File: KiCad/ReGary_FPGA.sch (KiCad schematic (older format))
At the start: 26 parts, among them U1 10M02SCU169C8G, U2 LM1117-3.3

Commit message: Removed BGA FPGA
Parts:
- removed U1: 10M02SCU169C8G, ReGary:BGA-169_11.0x11.0mm_Layout13x13_P0.8mm_Ball0.5mm_Pad0.35mm_NSMD, symbol ReGary:10M02SCU169
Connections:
- net labels removed: A0_FPGA, A1_FPGA, A2_FPGA, A3_FPGA, ABOE0_FPGA, ABOE1_FPGA, ABOE2_FPGA, ADDRZ3_FPGA, AS_FPGA, BERR_FPGA, BGACK_FPGA, BG_FPGA, BIGZ_FPGA, BINT_FPGA, BR_FPGA, C7M_FPGA, CBACK_FPGA, CBREQ_FPGA, CCS_FPGA, CDAC_FPGA, CIIN_FPGA, CINH_FPGA, CLK90_FPGA, CPUCLK_FPGA, D2P_FPGA, DBLT_FPGA, DBOE0_FPGA, DBOE1_FPGA, DBR16_FPGA, DOE_FPGA, DSACK0_FPGA, DSACK1_FPGA, DS_FPGA, DTACK_FPGA, EA2_FPGA, EA3_FPGA, EBCLR_FPGA, EBG0_FPGA, EBG1_FPGA, EBG2_FPGA, EBG3_FPGA, EBG4_FPGA, EBGACK_FPGA, EBR0_FPGA, EBR1_FPGA, EBR2_FPGA, EBR3_FPGA, EBR4_FPGA, EDS0_FPGA, EDS1_FPGA, EDS2_FPGA, EDS3_FPGA, FCS_FPGA, HLT_FPGA, IOZ2_FPGA, LOCK_EA1_FPGA, MEMZ2_FPGA, MS0_FPGA, MS1_FPGA, MS2_FPGA, MTACK_FPGA, MTCR_FPGA, OWN_FPGA, READ_FPGA, RESET_FPGA, RMC_FPGA, RW_FPGA, SBG_FPGA, SBR_FPGA, SIZ0_FPGA, SIZ1_FPGA, SLAVE0_FPGA, SLAVE1_FPGA, SLAVE2_FPGA, SLAVE3_FPGA, SLAVE4_FPGA, STERM_FPGA, WAIT_FPGA
- wire segments 82 -> 42
- no-connect marks 24 -> 3
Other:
- moved on the sheet: TP1

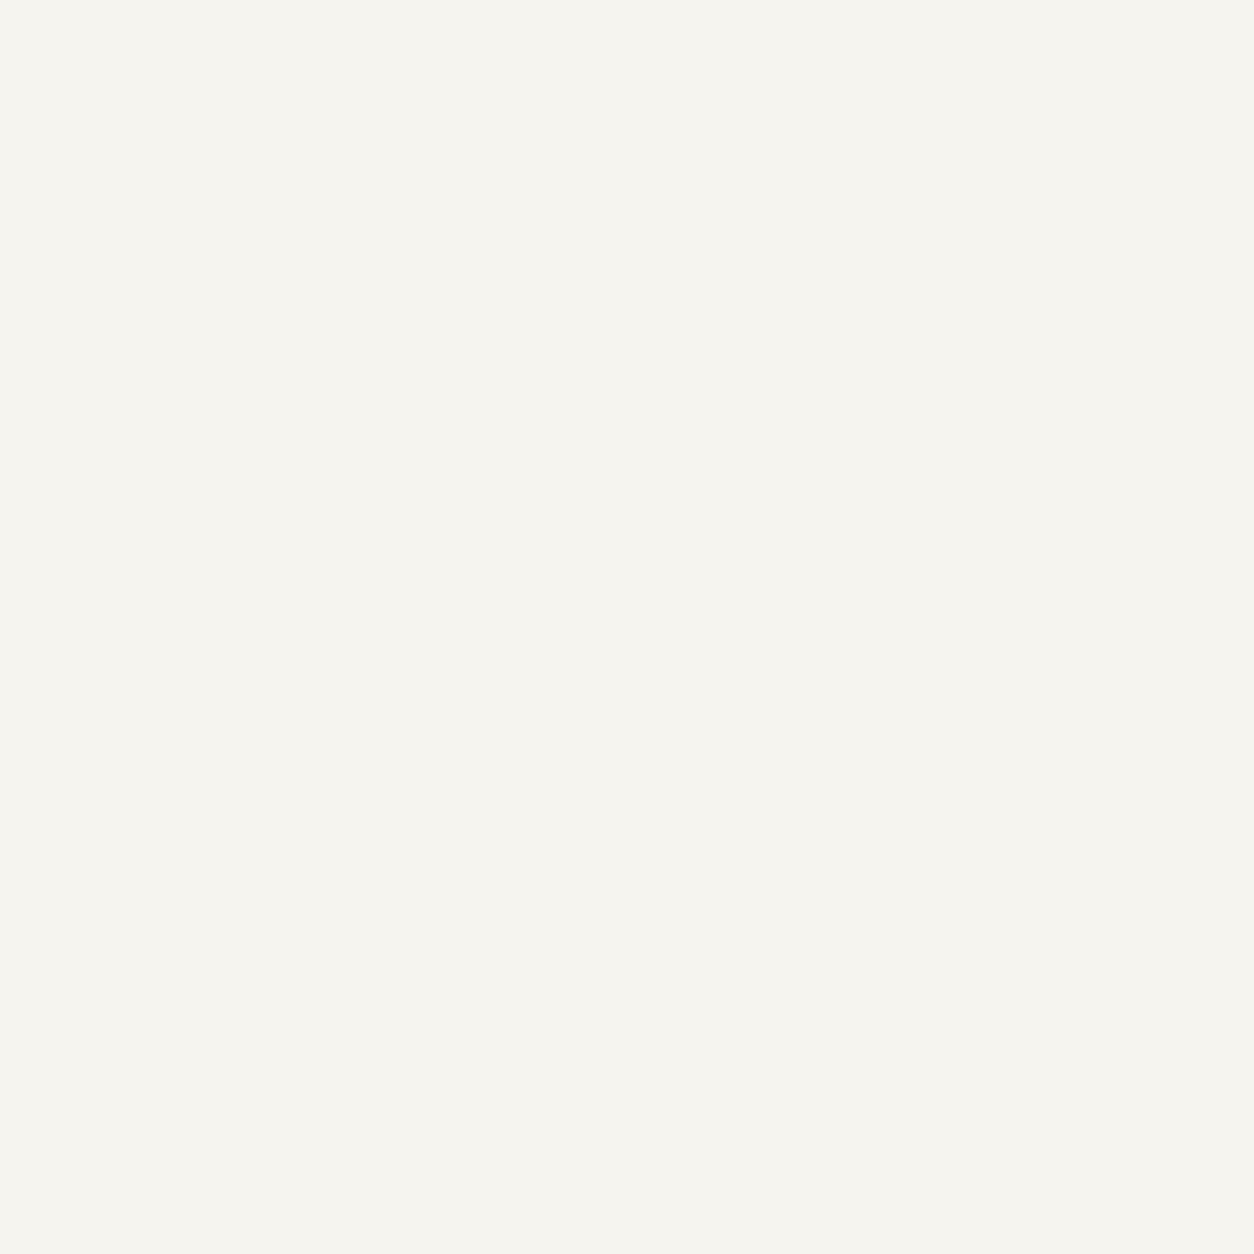
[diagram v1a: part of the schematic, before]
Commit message: Add Gowin FPGA GW1N-UV1P5LQ100 into the design
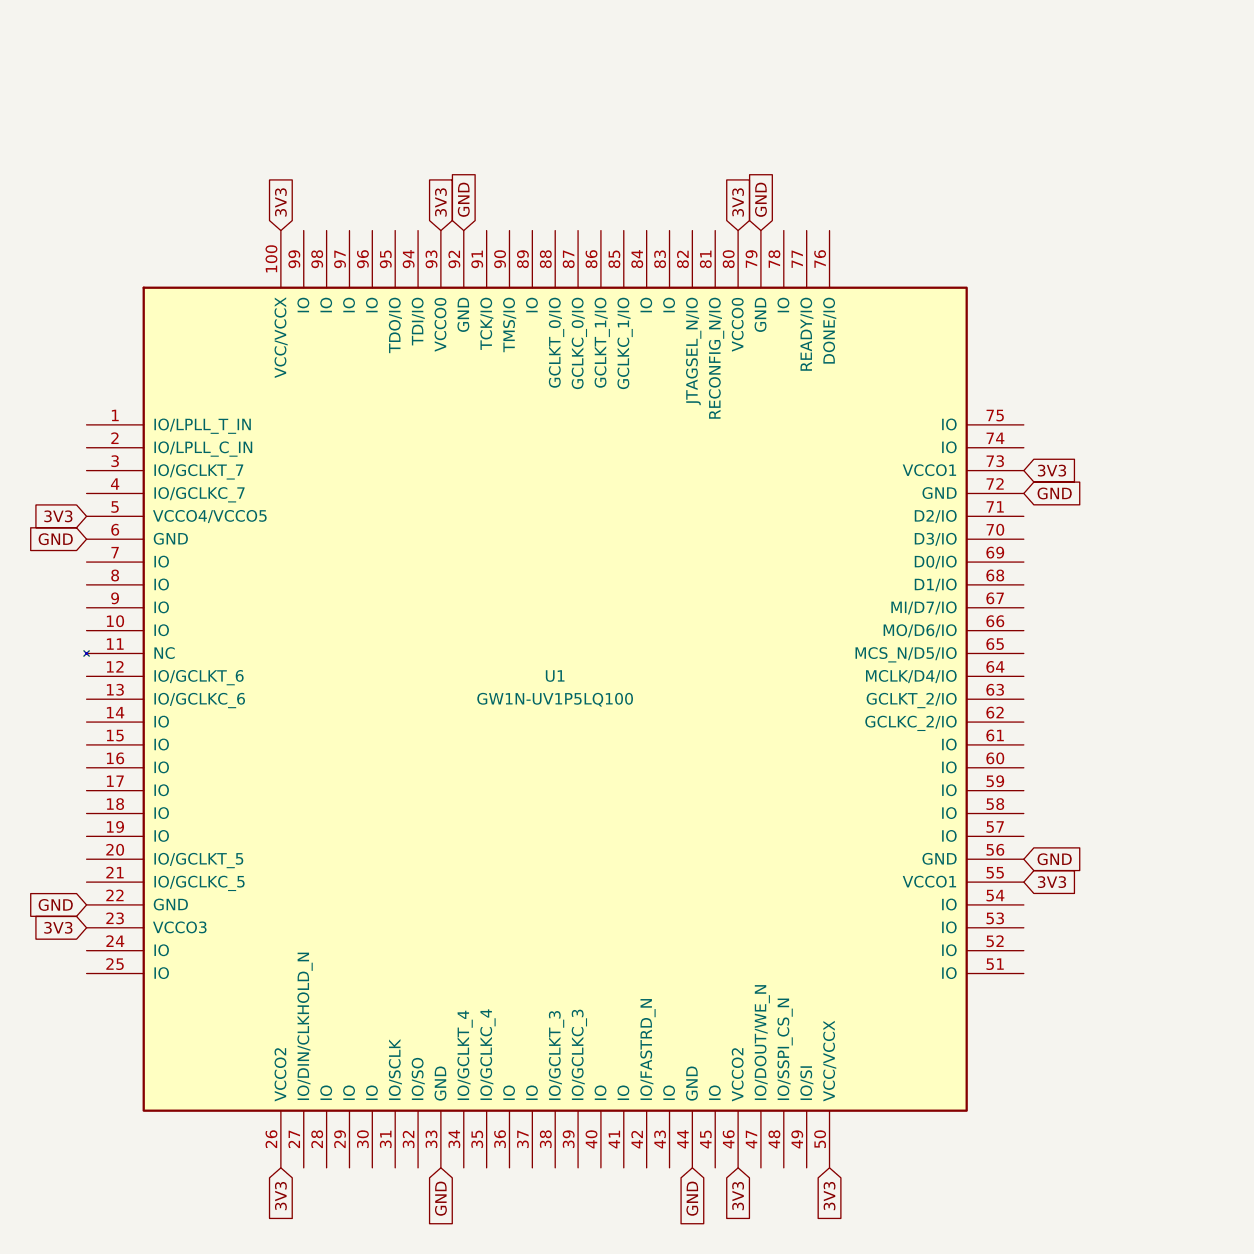
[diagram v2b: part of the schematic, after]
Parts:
- added U1: GW1N-UV1P5LQ100, Package_QFP:TQFP-100_14x14mm_P0.5mm, symbol ReGary:GW1N-UV1P5LQ100
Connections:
- net 3V3: now also U1.100 (VCC/VCCX), U1.23 (VCCO3), U1.26 (VCCO2), U1.46 (VCCO2), U1.5 (VCCO4/VCCO5), U1.50 (VCC/VCCX), U1.55 (VCCO1), U1.73 (VCCO1), U1.80 (VCCO0), U1.93 (VCCO0)
- net GND: now also U1.22 (GND), U1.33 (GND), U1.44 (GND), U1.56 (GND), U1.6 (GND), U1.72 (GND), U1.79 (GND), U1.92 (GND)
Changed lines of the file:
@@
 Wire Wire Line
 	7950 5300 8300 5300
+$Comp
+L ReGary:GW1N-UV1P5LQ100 U1
+U 1 1 67C4A39D
+P 3400 4150
+F 0 "U1" H 3400 4250 50  0000 C CNN
+F 1 "GW1N-UV1P5LQ100" H 3400 4150 50  0000 C CNN
+F 2 "Package_QFP:TQFP-100_14x14mm_P0.5mm" H 3400 4150 50  0001 C CNN
+F 3 "" H 3400 4150 50  0001 C CNN
+	1    3400 4150
+	1    0    0    -1
+$EndComp
+Text GLabel 4200 2100 1    50   Input ~ 0
+3V3
+Text GLabel 2900 2100 1    50   Input ~ 0
+3V3
+Text GLabel 2200 2100 1    50   Input ~ 0
+3V3
+Text GLabel 1350 3350 0    50   Input ~ 0
+3V3
+Text GLabel 1350 5150 0    50   Input ~ 0
+3V3
+Text GLabel 2200 6200 3    50   Input ~ 0
+3V3
+Text GLabel 4200 6200 3    50   Input ~ 0
+3V3
+Text GLabel 4600 6200 3    50   Input ~ 0
+3V3
+Text GLabel 5450 4950 2    50   Input ~ 0
+3V3
+Text GLabel 5450 3150 2    50   Input ~ 0
+3V3
+Text GLabel 1350 3450 0    50   Input ~ 0
+GND
+Text GLabel 1350 5050 0    50   Input ~ 0
+GND
+Text GLabel 2900 6200 3    50   Input ~ 0
+GND
+Text GLabel 4000 6200 3    50   Input ~ 0
+GND
+Text GLabel 5450 4850 2    50   Input ~ 0
+GND
+Text GLabel 5450 3250 2    50   Input ~ 0
+GND
+Text GLabel 4300 2100 1    50   Input ~ 0
+GND
+Text GLabel 3000 2100 1    50   Input ~ 0
+GND
 $EndSCHEMATC

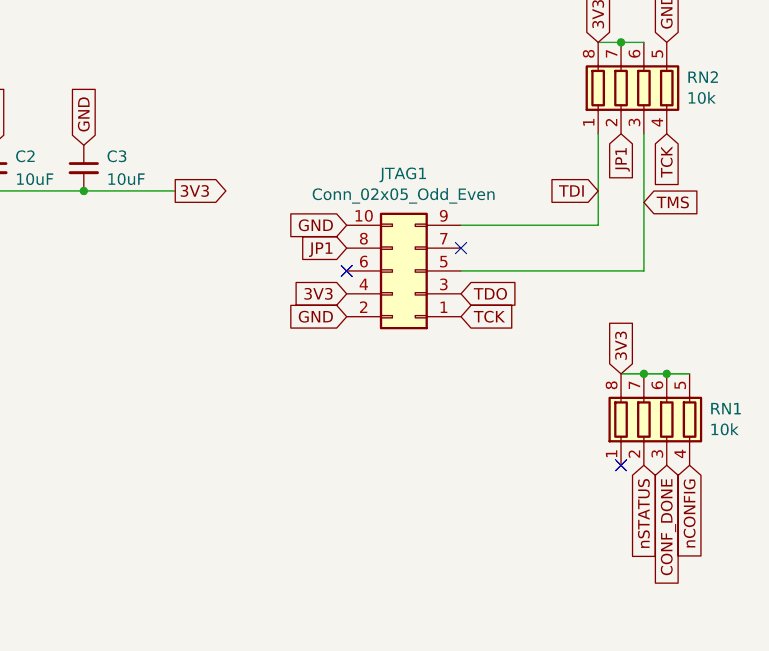
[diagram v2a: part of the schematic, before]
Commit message: Change to 6-pin JTAG-header
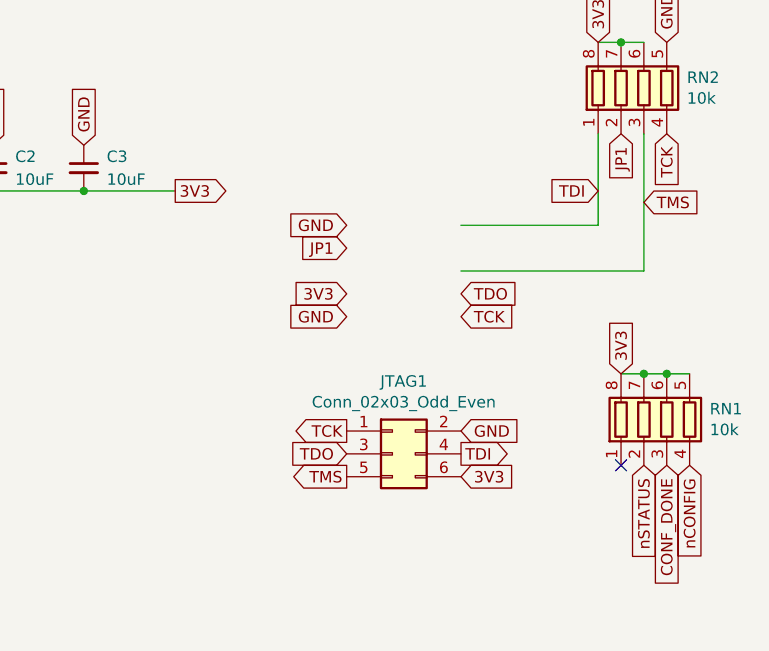
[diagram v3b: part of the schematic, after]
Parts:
- removed JTAG1: Conn_02x05_Odd_Even, Connector_PinHeader_2.00mm:PinHeader_2x05_P2.00mm_Vertical_SMD, symbol Connector_Generic:Conn_02x05_Odd_Even
- added JTAG1: Conn_02x03_Odd_Even, Connector_PinHeader_2.00mm:PinHeader_2x03_P2.00mm_Vertical_SMD, symbol Connector_Generic:Conn_02x03_Odd_Even
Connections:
- no-connect marks 3 -> 1
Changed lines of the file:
@@
 	7550 1500 7700 1500
 Connection ~ 7700 1500
-$Comp
-L Connector_Generic:Conn_02x05_Odd_Even JTAG1
-U 1 1 60C7D841
-P 9550 1850
-F 0 "JTAG1" H 9600 1425 50  0000 C CNN
-F 1 "Conn_02x05_Odd_Even" H 9600 1516 50  0000 C CNN
-F 2 "Connector_PinHeader_2.00mm:PinHeader_2x05_P2.00mm_Vertical_SMD" H 9550 1850 50  0001 C CNN
-F 3 "~" H 9550 1850 50  0001 C CNN
-	1    9550 1850
-	-1   0    0    1
-$EndComp
 Text GLabel 9250 1650 0    50   Input ~ 0
 GND
-NoConn ~ 9250 1850
 Text GLabel 9250 1950 0    50   Input ~ 0
 3V3
@@
 	10550 1250 10550 1850
 NoConn ~ 10450 2700
-NoConn ~ 9750 1750
 $Comp
 L Device:C C?
@@
 Text GLabel 3000 2100 1    50   Input ~ 0
 GND
+$Comp
+L Connector_Generic:Conn_02x03_Odd_Even JTAG1
+U 1 1 67CA7A4E
+P 9450 2650
+F 0 "JTAG1" H 9500 2967 50  0000 C CNN
+F 1 "Conn_02x03_Odd_Even" H 9500 2876 50  0000 C CNN
+F 2 "Connector_PinHeader_2.00mm:PinHeader_2x03_P2.00mm_Vertical_SMD" H 9450 2650 50  0001 C CNN
+F 3 "~" H 9450 2650 50  0001 C CNN
+	1    9450 2650
+	1    0    0    -1
+$EndComp
+Text GLabel 9250 2550 0    50   Output ~ 0
+TCK
+Text GLabel 9250 2650 0    50   Input ~ 0
+TDO
+Text GLabel 9250 2750 0    50   Output ~ 0
+TMS
+Text GLabel 9750 2550 2    50   Input ~ 0
+GND
+Text GLabel 9750 2650 2    50   Output ~ 0
+TDI
+Text GLabel 9750 2750 2    50   Input ~ 0
+3V3
 $EndSCHEMATC

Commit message: Add a 4V3 LDO voltage regulator
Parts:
- added U9: TPS73643DBV, Package_TO_SOT_SMD:SOT-23-5, symbol Regulator_Linear:TPS73643DBV
- C20: renamed from C6; footprint Capacitor_SMD:C_0805_2012Metric_Pad1.15x1.40mm_HandSolder -> Capacitor_SMD:C_0603_1608Metric_Pad1.08x0.95mm_HandSolder; symbol Device:C -> Device:C_Small
- C3: symbol Device:C_Small -> Device:C
- C4: symbol Device:C -> Device:C_Small
- renumbered C20 to C6
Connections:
- net labels added: 4V3
- wire segments 42 -> 53
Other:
- moved on the sheet: C20, C3, C4
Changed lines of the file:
@@
 P 10050 3750
 AR Path="/60CC8EF6" Ref="C?"  Part="1"
-AR Path="/608A10F5/60CC8EF6" Ref="C20"  Part="1"
-F 0 "C20" H 10150 3750 50  0000 L CNN
+AR Path="/608A10F5/60CC8EF6" Ref="C6"  Part="1"
+F 0 "C6" H 10150 3750 50  0000 L CNN
 F 1 "0.1uF" H 10050 3650 50  0000 L CNN
 F 2 "Capacitor_SMD:C_0603_1608Metric_Pad1.05x0.95mm_HandSolder" H 10088 3600 50  0001 C CNN
@@
 $EndComp
 $Comp
-L Device:C C?
+L Device:C_Small C?
 U 1 1 6085C631
-P 7250 5150
+P 4750 1100
 AR Path="/6085C631" Ref="C?"  Part="1"
 AR Path="/608A10F5/6085C631" Ref="C4"  Part="1"
-F 0 "C4" H 7350 5150 50  0000 L CNN
-F 1 "1uF" H 7250 5050 50  0000 L CNN
-F 2 "Capacitor_SMD:C_0805_2012Metric_Pad1.15x1.40mm_HandSolder" H 7288 5000 50  0001 C CNN
-F 3 "~" H 7250 5150 50  0001 C CNN
-	1    7250 5150
-	1    0    0    -1
-$EndComp
-$Comp
-L Device:C_Small C3
+F 0 "C4" H 4550 1100 50  0000 L CNN
+F 1 "1uF" H 4600 1200 50  0000 L CNN
+F 2 "Capacitor_SMD:C_0805_2012Metric_Pad1.15x1.40mm_HandSolder" H 4788 950 50  0001 C CNN
+F 3 "~" H 4750 1100 50  0001 C CNN
+	1    4750 1100
+	-1   0    0    1
+$EndComp
+$Comp
+L Device:C C3
 U 1 1 6086B673
-P 8100 1400
-F 0 "C3" H 8200 1450 50  0000 L CNN
-F 1 "10uF" H 8200 1350 50  0000 L CNN
-F 2 "Capacitor_SMD:C_1206_3216Metric_Pad1.42x1.75mm_HandSolder" H 8100 1400 50  0001 C CNN
-F 3 "~" H 8100 1400 50  0001 C CNN
-	1    8100 1400
-	1    0    0    -1
-$EndComp
-Wire Wire Line
-	7700 1500 8100 1500
-Connection ~ 8100 1500
-Wire Wire Line
-	8100 1500 8500 1500
+P 3450 1150
+F 0 "C3" H 3550 1200 50  0000 L CNN
+F 1 "10uF" H 3550 1100 50  0000 L CNN
+F 2 "Capacitor_SMD:C_1206_3216Metric_Pad1.42x1.75mm_HandSolder" H 3450 1150 50  0001 C CNN
+F 3 "~" H 3450 1150 50  0001 C CNN
+	1    3450 1150
+	-1   0    0    1
+$EndComp
 Text GLabel 7500 2600 0    50   Input ~ 0
 TP1
@@
 NoConn ~ 10450 2700
 $Comp
-L Device:C C?
+L Device:C_Small C?
 U 1 1 60785965
-P 7250 4450
+P 4450 1150
 AR Path="/60785965" Ref="C?"  Part="1"
-AR Path="/608A10F5/60785965" Ref="C6"  Part="1"
-F 0 "C6" H 7350 4450 50  0000 L CNN
-F 1 "0.1uF" H 7250 4350 50  0000 L CNN
-F 2 "Capacitor_SMD:C_0805_2012Metric_Pad1.15x1.40mm_HandSolder" H 7288 4300 50  0001 C CNN
-F 3 "~" H 7250 4450 50  0001 C CNN
-	1    7250 4450
+AR Path="/608A10F5/60785965" Ref="C20"  Part="1"
+F 0 "C20" H 4500 1100 50  0000 L CNN
+F 1 "0.1uF" H 4450 1000 50  0000 L CNN
+F 2 "Capacitor_SMD:C_0603_1608Metric_Pad1.08x0.95mm_HandSolder" H 4488 1000 50  0001 C CNN
+F 3 "~" H 4450 1150 50  0001 C CNN
+	1    4450 1150
 	1    0    0    -1
 $EndComp
@@
 Text GLabel 9750 2750 2    50   Input ~ 0
 3V3
+$Comp
+L Regulator_Linear:TPS73643DBV U9
+U 1 1 67D103CA
+P 4050 1050
+F 0 "U9" H 4050 1417 50  0000 C CNN
+F 1 "TPS73643DBV" H 4050 1326 50  0000 C CNN
+F 2 "Package_TO_SOT_SMD:SOT-23-5" H 4050 1375 50  0001 C CIN
+F 3 "http://www.ti.com/lit/ds/symlink/tps736.pdf" H 4050 1000 50  0001 C CNN
+	1    4050 1050
+	1    0    0    -1
+$EndComp
+Text GLabel 3450 950  0    50   Input ~ 0
+VCC
+Wire Wire Line
+	3650 950  3450 950
+Wire Wire Line
+	7700 1500 8500 1500
+Wire Wire Line
+	3450 1350 4050 1350
+Text GLabel 4050 1350 3    50   Input ~ 0
+GND
+Text GLabel 5100 950  2    50   Output ~ 0
+4V3
+Wire Wire Line
+	3650 1050 3650 950
+Connection ~ 3650 950
+Wire Wire Line
+	4450 950  4750 950
+Wire Wire Line
+	3450 1300 3450 1350
+Wire Wire Line
+	3450 950  3450 1000
+Wire Wire Line
+	4050 1350 4450 1350
+Wire Wire Line
+	4750 1350 4750 1200
+Connection ~ 4050 1350
+Wire Wire Line
+	4750 1000 4750 950
+Connection ~ 4750 950
+Wire Wire Line
+	4750 950  5100 950
+Wire Wire Line
+	4450 1250 4450 1350
+Connection ~ 4450 1350
+Wire Wire Line
+	4450 1350 4750 1350
 $EndSCHEMATC

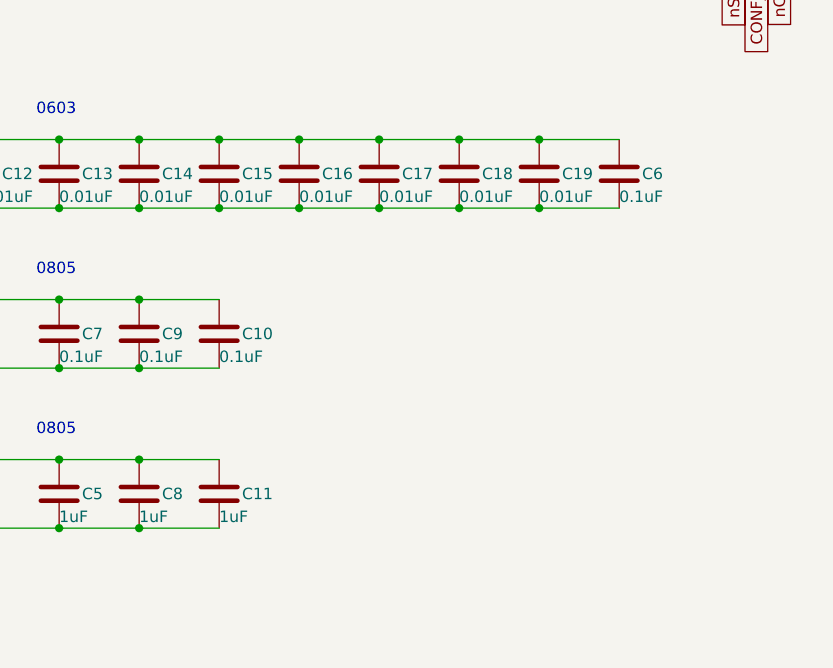
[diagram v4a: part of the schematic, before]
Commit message: Fixed placement of C5 and FPGA, more cleanup of old vias and traces
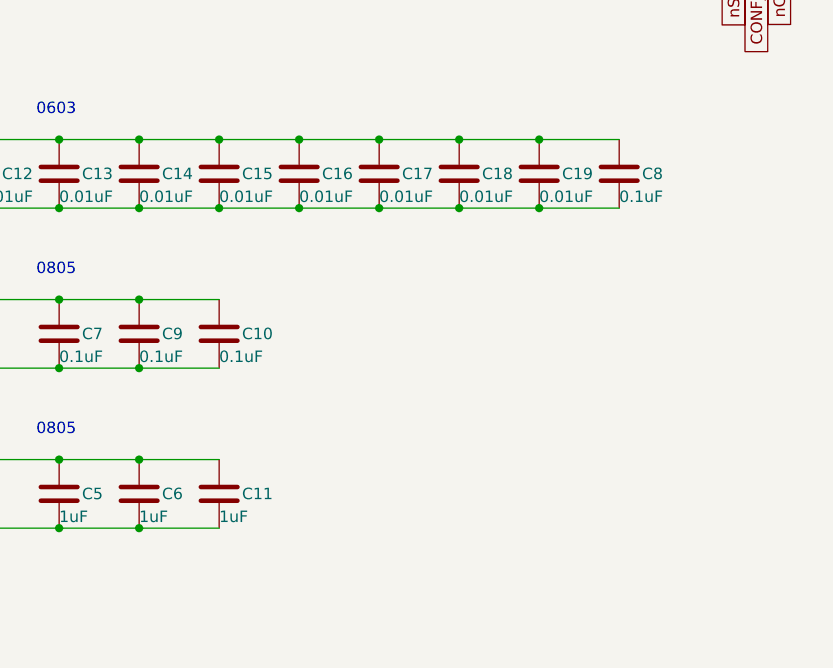
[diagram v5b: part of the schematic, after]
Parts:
- renumbered C8 to C6, C6 to C8
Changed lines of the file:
@@
 P 10050 3750
 AR Path="/60CC8EF6" Ref="C?"  Part="1"
-AR Path="/608A10F5/60CC8EF6" Ref="C6"  Part="1"
-F 0 "C6" H 10150 3750 50  0000 L CNN
+AR Path="/608A10F5/60CC8EF6" Ref="C8"  Part="1"
+F 0 "C8" H 10150 3750 50  0000 L CNN
 F 1 "0.1uF" H 10050 3650 50  0000 L CNN
 F 2 "Capacitor_SMD:C_0603_1608Metric_Pad1.05x0.95mm_HandSolder" H 10088 3600 50  0001 C CNN
@@
 P 7950 5150
 AR Path="/6084338C" Ref="C?"  Part="1"
-AR Path="/608A10F5/6084338C" Ref="C8"  Part="1"
-F 0 "C8" H 8050 5150 50  0000 L CNN
+AR Path="/608A10F5/6084338C" Ref="C6"  Part="1"
+F 0 "C6" H 8050 5150 50  0000 L CNN
 F 1 "1uF" H 7950 5050 50  0000 L CNN
 F 2 "Capacitor_SMD:C_0805_2012Metric_Pad1.15x1.40mm_HandSolder" H 7988 5000 50  0001 C CNN
